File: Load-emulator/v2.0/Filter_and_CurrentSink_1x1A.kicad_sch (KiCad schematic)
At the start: 11 parts, among them Q9 RD3L08DBLHRB, U15 LT1492, U17 INA185

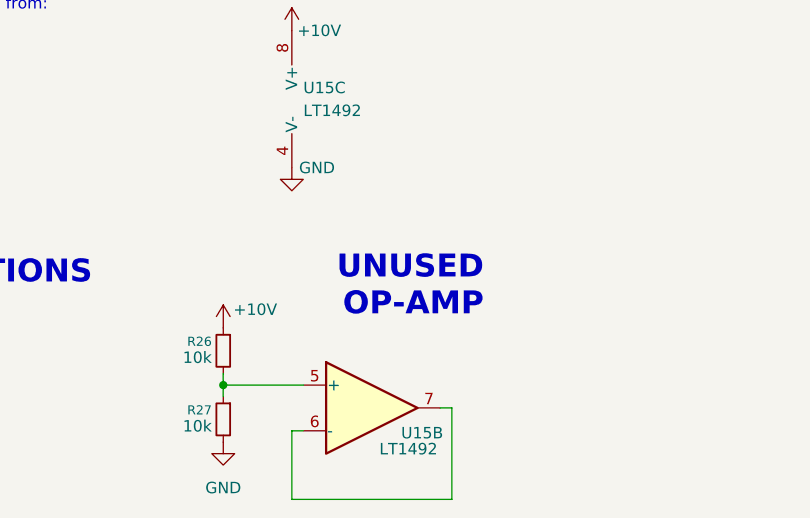
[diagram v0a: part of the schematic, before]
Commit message: [v2.0 - WIP] Added PCB Sketch
[REMOVED]
 - Some comments;

[ADDED]
- 3D models for some components, like heatsinks;
- PCB Sketch (This is just to review how it will look);
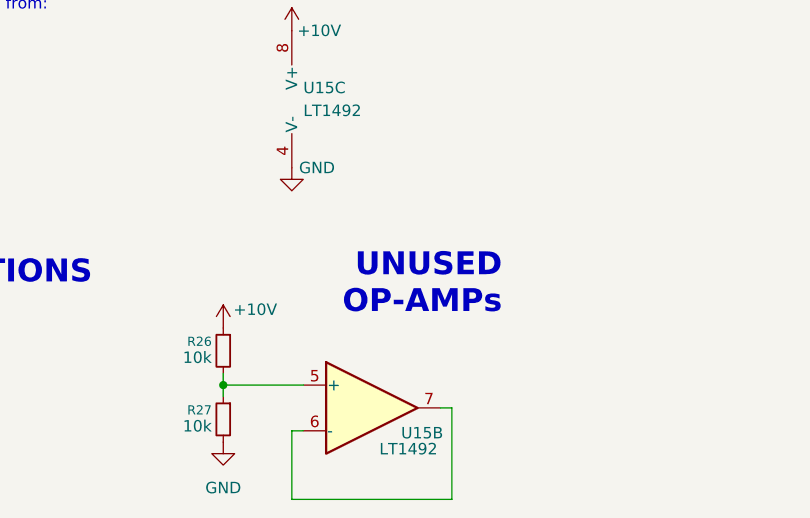
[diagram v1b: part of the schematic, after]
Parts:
- R26, R27: footprint (none) -> Resistor_SMD:R_0603_1608Metric
- U15: footprint (none) -> footprints:SO-8_S_LIT
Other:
- note added: "UNUSED OP-AMPs"
- note removed: "UNUSED OP-AMP"
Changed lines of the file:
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@@
 	(title_block
 		(title "Load Emulator")
-		(date "2025-09-28")
+		(date "2025-10-03")
 		(rev "v2.0 - WIP")
 		(company "Spacelab")
@@
 		)
 	)
-	(text "UNUSED\nOP-AMP"
-		(exclude_from_sim no)
-		(at 97.536 167.132 0)
+	(text "UNUSED\nOP-AMPs"
+		(exclude_from_sim no)
+		(at 99.568 166.878 0)
 		(effects
 			(font
@@
 	(wire
 		(pts
+			(xy 147.32 43.18) (xy 147.32 54.61)
+		)
+		(stroke
+			(width 0)
+			(type default)
+		)
+	)
+	(wire
+		(pts
 			(xy 77.47 186.69) (xy 76.2 186.69)
 		)
@@
 	(wire
 		(pts
+			(xy 147.32 43.18) (xy 149.86 43.18)
+		)
+		(stroke
+			(width 0)
+			(type default)
+		)
+	)
+	(wire
+		(pts
 			(xy 184.15 54.61) (xy 184.15 57.15)
 		)
@@
 	(wire
 		(pts
-			(xy 147.32 43.18) (xy 147.32 54.61)
-		)
-		(stroke
-			(width 0)
-			(type default)
-		)
-	)
-	(wire
-		(pts
 			(xy 93.98 184.15) (xy 92.71 184.15)
 		)
@@
 	(wire
 		(pts
+			(xy 147.32 54.61) (xy 184.15 54.61)
+		)
+		(stroke
+			(width 0)
+			(type default)
+		)
+	)
+	(wire
+		(pts
 			(xy 54.61 39.37) (xy 59.69 39.37)
 		)
@@
 	(wire
 		(pts
-			(xy 147.32 54.61) (xy 184.15 54.61)
-		)
-		(stroke
-			(width 0)
-			(type default)
-		)
-	)
-	(wire
-		(pts
 			(xy 35.56 39.37) (xy 40.64 39.37)
 		)
@@
 		(pts
 			(xy 226.06 64.77) (xy 226.06 63.5)
-		)
-		(stroke
-			(width 0)
-			(type default)
-		)
-	)
-	(wire
-		(pts
-			(xy 147.32 43.18) (xy 149.86 43.18)
 		)
 		(stroke
@@
 		(polyline
 			(pts
-				(xy 121.285 20.32) (xy 203.835 20.32) (xy 203.835 71.12) (xy 121.285 71.12)
+				(xy 12.7 132.3975) (xy 57.15 132.3975) (xy 57.15 164.7825) (xy 12.7 164.7825)
 			)
 			(stroke
@@
 		(polyline
 			(pts
-				(xy 12.7 130.81) (xy 12.7 102.87) (xy 57.15 102.87) (xy 57.15 130.81)
+				(xy 58.42 132.3974) (xy 93.98 132.3975) (xy 93.98 164.7825) (xy 58.42 164.7824)
 			)
 			(stroke
@@
 		(polyline
 			(pts
-				(xy 95.885 20.32) (xy 95.885 63.5) (xy 20.955 63.5) (xy 20.955 20.32)
+				(xy 121.285 20.32) (xy 203.835 20.32) (xy 203.835 71.12) (xy 121.285 71.12)
 			)
 			(stroke
@@
 		(polyline
 			(pts
-				(xy 12.7 132.3975) (xy 57.15 132.3975) (xy 57.15 164.7825) (xy 12.7 164.7825)
+				(xy 221.615 45.72) (xy 268.605 45.72) (xy 268.605 99.06) (xy 221.615 99.06)
+			)
+			(stroke
+				(width 0.25)
+				(type dash)
+				(color 255 0 0 1)
+			)
+			(fill
+				(type none)
+			)
+		)
+	)
+	(rule_area
+		(polyline
+			(pts
+				(xy 12.7 130.81) (xy 12.7 102.87) (xy 57.15 102.87) (xy 57.15 130.81)
 			)
 			(stroke
@@
 		(polyline
 			(pts
-				(xy 12.7 165.4174) (xy 57.15 165.4174) (xy 57.15 197.8024) (xy 12.7 197.8024)
+				(xy 58.4721 165.4336) (xy 100.3299 165.4174) (xy 100.3299 197.8024) (xy 58.4721 197.8186)
 			)
 			(stroke
@@
 		(polyline
 			(pts
-				(xy 58.42 132.3974) (xy 93.98 132.3975) (xy 93.98 164.7825) (xy 58.42 164.7824)
+				(xy 12.7 165.4174) (xy 57.15 165.4174) (xy 57.15 197.8024) (xy 12.7 197.8024)
 			)
 			(stroke
@@
 		(polyline
 			(pts
-				(xy 58.42 165.4175) (xy 97.79 165.4175) (xy 97.79 197.8025) (xy 58.42 197.8025)
+				(xy 95.885 20.32) (xy 95.885 63.5) (xy 20.955 63.5) (xy 20.955 20.32)
 			)
 			(stroke
@@
 				(type dash)
 				(color 0 0 0 1)
-			)
-			(fill
-				(type none)
-			)
-		)
-	)
-	(rule_area
-		(polyline
-			(pts
-				(xy 221.615 45.72) (xy 268.605 45.72) (xy 268.605 99.06) (xy 221.615 99.06)
-			)
-			(stroke
-				(width 0.25)
-				(type dash)
-				(color 255 0 0 1)
 			)
 			(fill
@@
 			)
 		)
-		(property "Footprint" ""
+		(property "Footprint" "Resistor_SMD:R_0603_1608Metric"
 			(at 68.58 177.8 0)
 			(effects
@@
 			)
 		)
-		(property "Footprint" ""
+		(property "Footprint" "footprints:SO-8_S_LIT"
 			(at 85.09 184.15 0)
 			(effects
@@
 			)
 		)
-		(property "Footprint" ""
+		(property "Footprint" "footprints:SO-8_S_LIT"
 			(at 78.74 149.86 0)
 			(effects
@@
 			)
 		)
-		(property "Footprint" ""
+		(property "Footprint" "footprints:SO-8_S_LIT"
 			(at 157.48 40.64 0)
 			(effects
@@
 			)
 		)
-		(property "Footprint" ""
+		(property "Footprint" "Resistor_SMD:R_0603_1608Metric"
 			(at 68.58 185.42 0)
 			(effects

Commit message: [v2.0 - WIP] Release Candidate 1. (#6)
Ready for review
- PCB Wired up.
- Schematic ready.

[MISSING]
- Values for some Resistors and Capacitors;
- Verify if EPS conector is correct;
- Change schematic to release.
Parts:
- removed U17: INA185, Package_TO_SOT_SMD:SOT-563, symbol Amplifier_Current:INA185
- C14: renamed from C37; footprint Capacitor_SMD:C_0201_0603Metric -> Capacitor_SMD:C_0805_2012Metric
- C15: renamed from C38; footprint Capacitor_SMD:C_0201_0603Metric -> Capacitor_SMD:C_0805_2012Metric
- HS8: renamed from HS9; footprint (none) -> footprints:573100D00000G
- R50: renamed from R66; footprint Resistor_SMD:R_0201_0603Metric -> Resistor_SMD:R_0603_1608Metric
- R51: renamed from R67; footprint Resistor_SMD:R_0201_0603Metric -> Resistor_SMD:R_0603_1608Metric
- R54: renamed from R68; footprint (none) -> Resistor_SMD:R_2512_6332Metric
- renumbered Q9 to Q8, R26 to R52, R27 to R53, U15 to U11
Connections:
- no-connect marks 1 -> 0
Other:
- note added: "Resistor in Current Sink choose from: Rsense = (Vcontrol/Ieps)/10 Rsense = PWM/1A"
- note removed: "CURRENT SENSOR"
- note removed: "It's gonna be necessary to do alot to get the readings from the sensors, gonna need a ADC converter for the i²C, asked by Joao."
- note removed: "NOT ON PROTOTYPE"
- note removed: "Resistor in Current Sink choose from: Ieps = Vcontrol/Rsense Rsense = Vcontrol/Ieps Rsense = PWM/1A"
- moved on the sheet: Q8, R54, U11A

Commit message: v2.0
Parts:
- C14, C15, R50, R51, R52, R53, R54: Type (none) -> SMD
- HS8: Manufacturer (none) -> Boyd Laconia, LLC; Manufacturer Order Number (none) -> 573100D00000G; Type (none) -> SMD
- Q8: Manufacturer (none) -> Rohm Semiconductor; Manufacturer Order Number (none) -> RD3L08DBLHRBTL; Type (none) -> SMD
- U11: Manufacturer (none) -> Analog Devices Inc.; Manufacturer Order Number (none) -> LT1492CS8#TRPBF; Type (none) -> SMD
